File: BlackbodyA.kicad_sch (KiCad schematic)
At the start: 0 parts

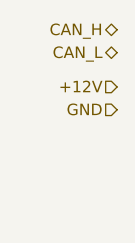
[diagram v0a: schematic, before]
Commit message: Updated contactors and added Blackbody C
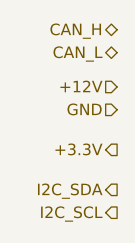
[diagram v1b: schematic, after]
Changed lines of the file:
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@@
 (kicad_sch (version 20230121) (generator eeschema)
   (paper "A4")
+  (hierarchical_label "+3.3V" (shape output) (at 100.965 93.98 180) (fields_autoplaced)
+    (effects (font (size 1.27 1.27)) (justify right))
+  )
   (hierarchical_label "CAN_H" (shape bidirectional) (at 100.965 80.645 180) (fields_autoplaced)
     (effects (font (size 1.27 1.27)) (justify right))
@@
     (effects (font (size 1.27 1.27)) (justify right))
   )
+  (hierarchical_label "I2C_SCL" (shape output) (at 100.965 100.965 180) (fields_autoplaced)
+    (effects (font (size 1.27 1.27)) (justify right))
+  )
   (hierarchical_label "GND" (shape input) (at 100.965 89.535 180) (fields_autoplaced)
     (effects (font (size 1.27 1.27)) (justify right))
   )
+  (hierarchical_label "I2C_SDA" (shape output) (at 100.965 98.425 180) (fields_autoplaced)
+    (effects (font (size 1.27 1.27)) (justify right))
+  )
